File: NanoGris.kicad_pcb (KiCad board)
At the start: 2 copper layers, 164.6 x 108 mm, 112 parts, among them J10 Conn_01x12, J11 Conn_01x12, J12 Conn_02x05_Odd_Even, J13 Conn_01x10, J14 Conn_01x10, J15 Conn_01x10, J16 Conn_01x03, J7 Conn_01x10, Q1 2N3904, Q2 2N3904, U1 MCP6002_1, U2 MCP6002_1, U3 MCP6002_1, U4 L7805, U5 LM4040LP-5, U6 74HC595, X1 CV_X, Y1 CV_Y

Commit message: Rename
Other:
- board text added: "NanoGris V0.041 By Quinie"
- board text removed: "NanoGrids V0.041 By Quinie"

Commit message: Bom Update (R31 needs to be 10K)
Error inBOM R31 needs to be 10k
https://www.quinie.nl/nanogris-big-bom-mistake-update-for-better-range-on-pots/
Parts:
- R31: value 100k -> 10k
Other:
- net class Default removed

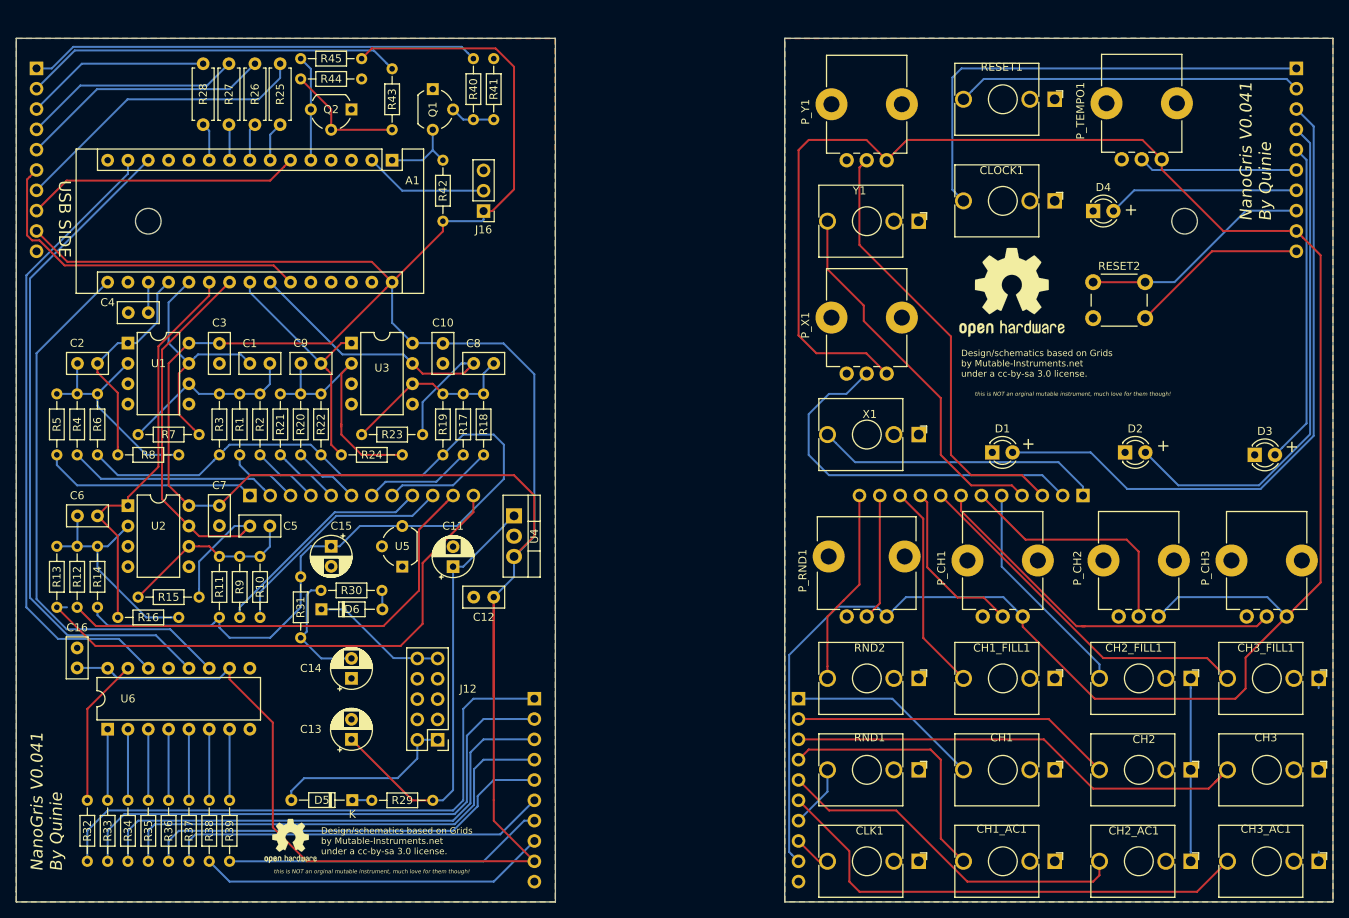
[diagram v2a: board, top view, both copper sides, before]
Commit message: Updated powerheader
Now with correct power schematic and boxed header.
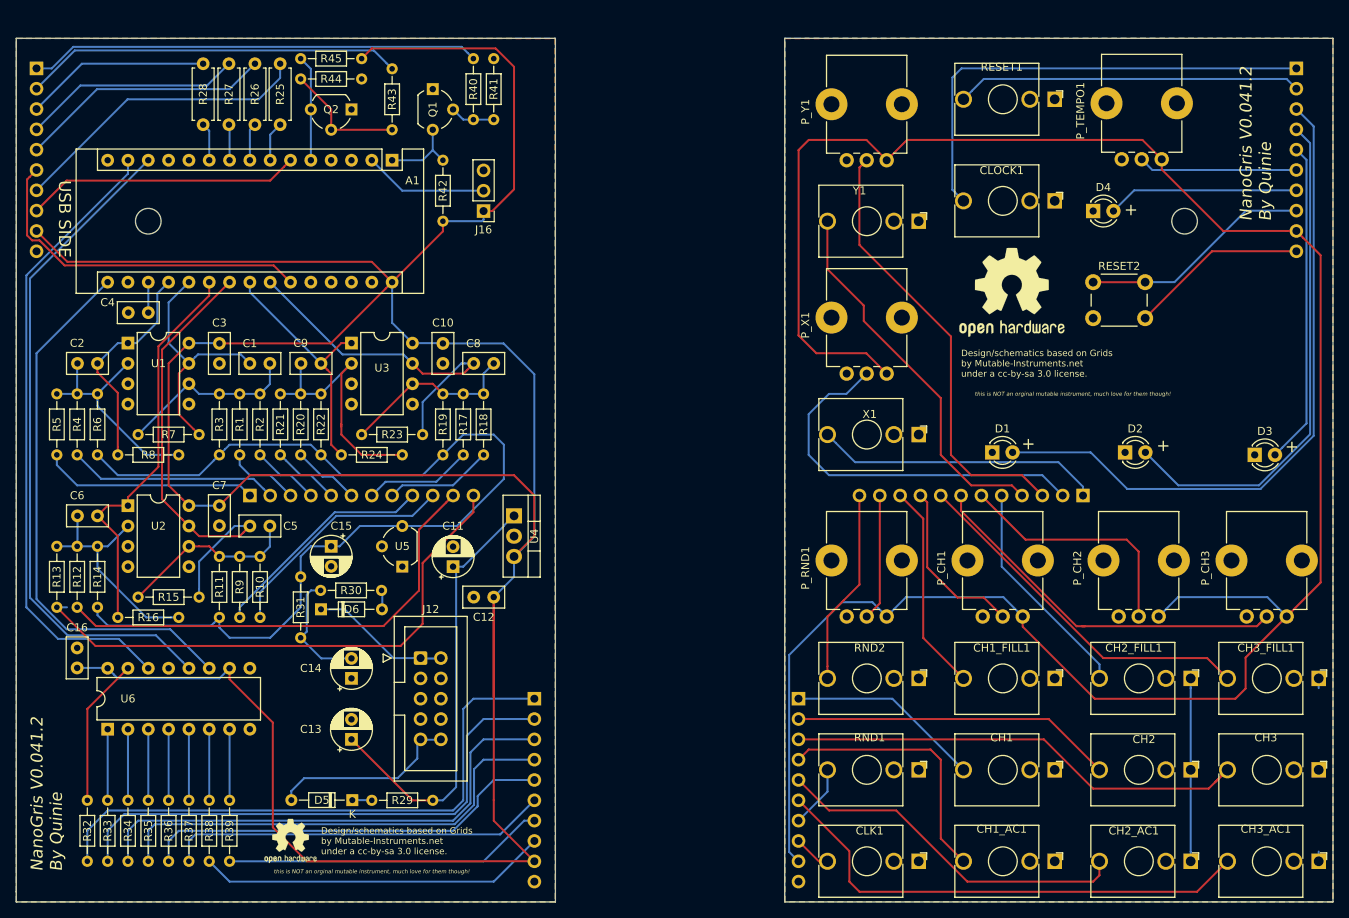
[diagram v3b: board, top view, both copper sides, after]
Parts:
- J12: footprint Connector_PinHeader_2.54mm:PinHeader_2x05_P2.54mm_Vertical -> Connector_IDC:IDC-Header_2x05_P2.54mm_Vertical
- P_CH1, P_CH2, P_CH3, P_TEMPO1, P_X1, P_Y1: footprint Potentiometer_THT:Potentiometer_Alps_RK09K_Single_Vertical -> Potentiometer_THT:Potentiometer_Alps_RK09K_Single_Vertical_round
- P_RND1: footprint Potentiometer_THT:Potentiometer_Alps_RK09L_Single_Vertical -> Potentiometer_THT:Potentiometer_Alps_RK09K_Single_Vertical_round
- moved J12 10.4 mm to (152.1, 95.2), turned to 0 degrees
- moved D6 0.05 mm to (139.7, 89.2)
- moved R30 0.05 mm to (147.3, 86.8)
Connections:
- A1 pad 11: Net-(A1-Pad11) -> unconnected-(A1-Pad11)
- A1 pad 12: Net-(A1-Pad12) -> unconnected-(A1-Pad12)
- A1 pad 15: Net-(A1-Pad15) -> unconnected-(A1-Pad15)
- A1 pad 17: Net-(A1-Pad17) -> unconnected-(A1-Pad17)
- A1 pad 26: Net-(A1-Pad26) -> unconnected-(A1-Pad26)
- A1 pad 27: Net-(A1-Pad27) -> unconnected-(A1-Pad27)
- A1 pad 28: Net-(A1-Pad28) -> unconnected-(A1-Pad28)
- A1 pad 3: Net-(A1-Pad3) -> unconnected-(A1-Pad3)
- J12 pad 1: Net-(D5-Pad2) -> Net-(D6-Pad1)
- J12 pad 10: Net-(D6-Pad1) -> Net-(D5-Pad2)
- J12 pad 2: Net-(D5-Pad2) -> Net-(D6-Pad1)
- J12 pad 9: Net-(D6-Pad1) -> Net-(D5-Pad2)
- U6 pad 9: Net-(U6-Pad9) -> unconnected-(U6-Pad9)
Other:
- board text added: "NanoGris V0.041.2 By Quinie"
- board text removed: "NanoGris V0.041 By Quinie"
